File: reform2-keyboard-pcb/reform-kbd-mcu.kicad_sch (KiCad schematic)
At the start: 31 parts, among them J1 USB, J2 UART, J3 AUX, J4 USB, SW83 RESET, SW84 SW_DIP_x01, U1 ATMEGA32U4-AU, U3 MCP1700-3302E_SOT23, Y1 16MHz

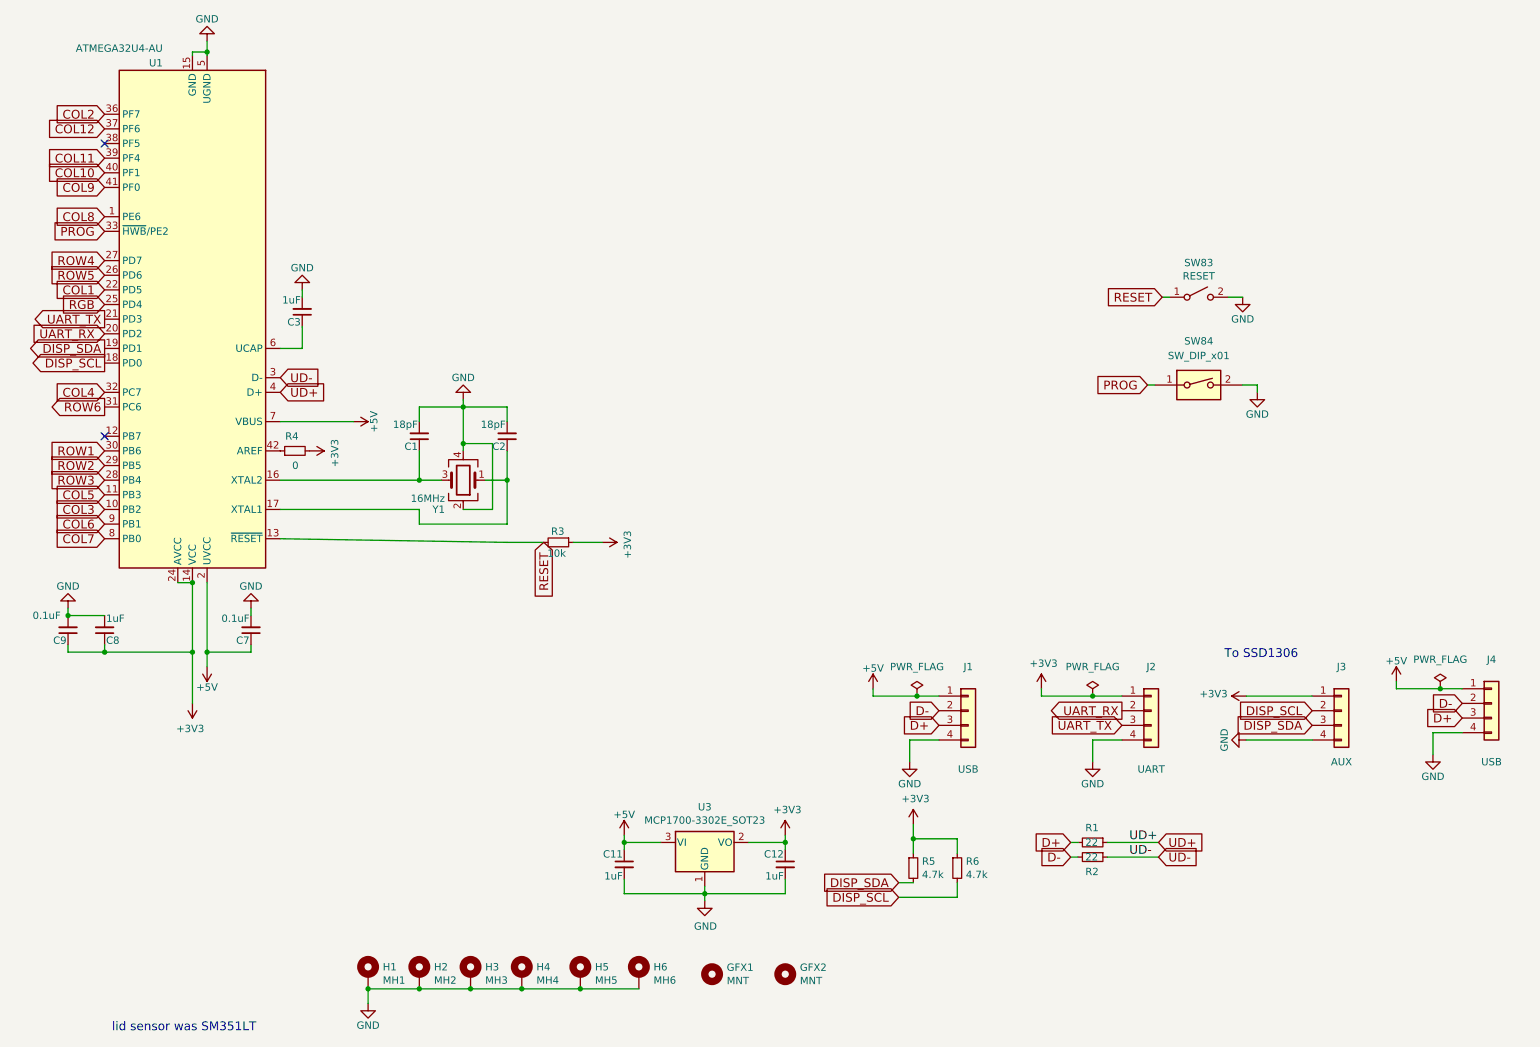
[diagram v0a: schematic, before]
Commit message: more routing of smd parts, add sockets
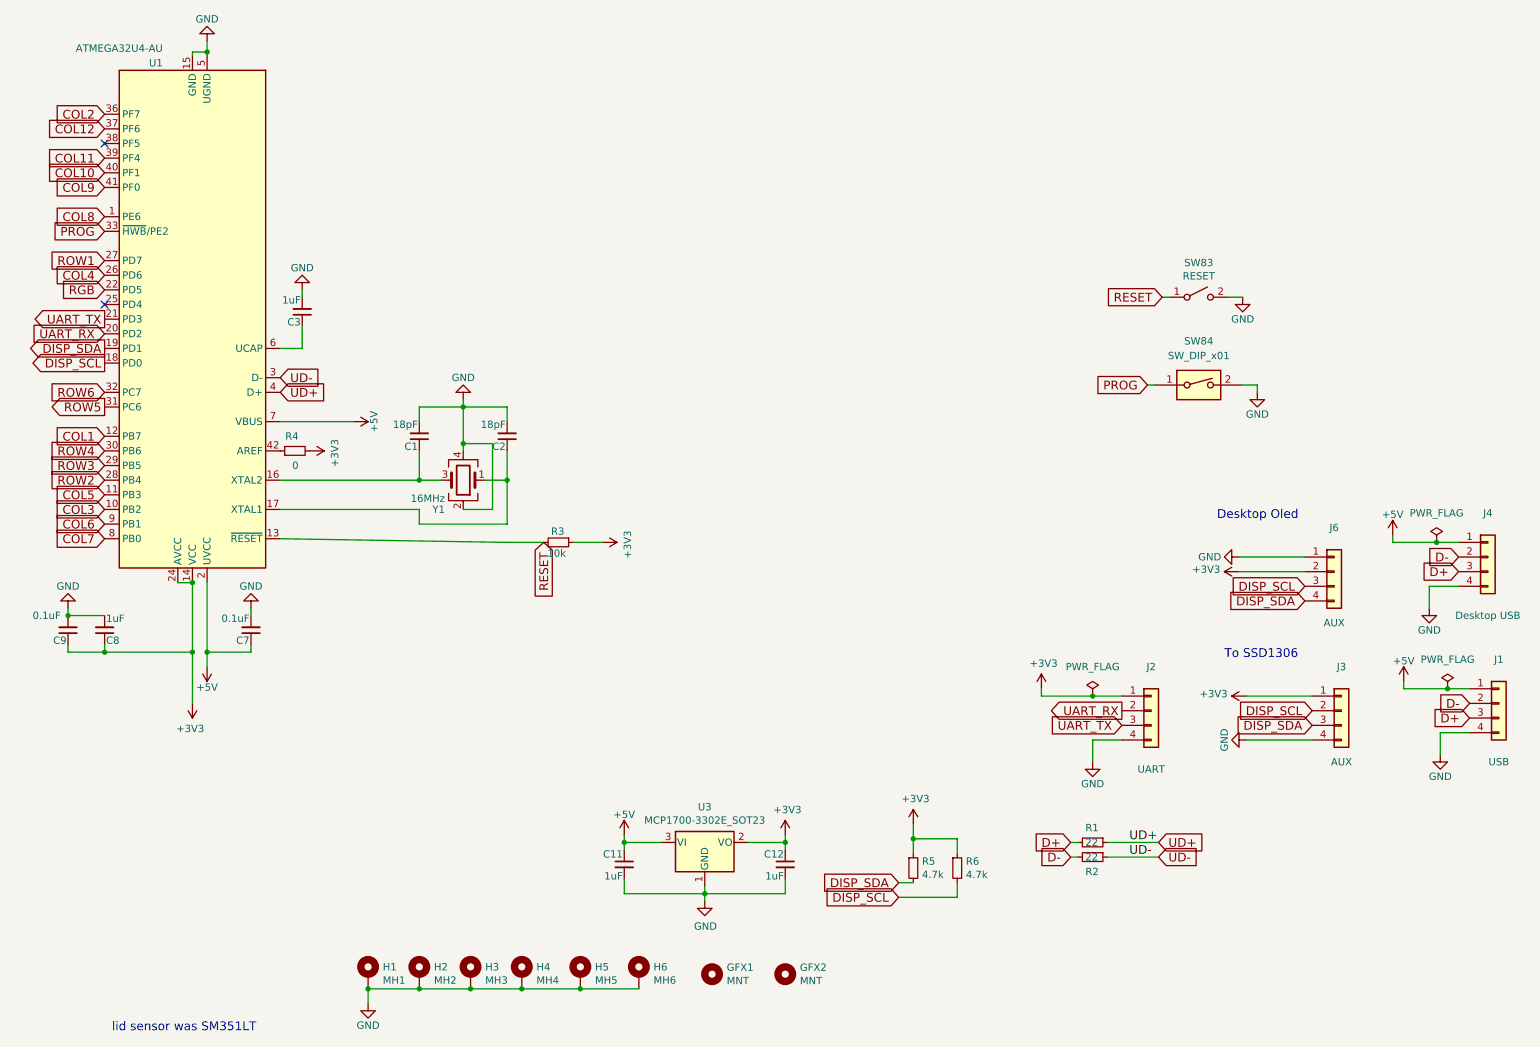
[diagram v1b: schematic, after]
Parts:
- added J6: AUX, Connector_PinHeader_2.54mm:PinHeader_1x04_P2.54mm_Vertical, symbol Connector_Generic:Conn_01x04
- J4: value USB -> Desktop USB; Manufacturer JST -> (none); Manufacturer_No S4B-PH-SM4-TB(LF)(SN) -> IDC 2.54 header 1x04
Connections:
- net +3V3: now also J6.2 (Pin_2)
- net COL1: now also U1.12 (PB7); no longer U1.22 (PD5)
- net COL4: now also U1.26 (PD6); no longer U1.32 (PC7)
- net DISP_SCL: now also J6.3 (Pin_3)
- net DISP_SDA: now also J6.4 (Pin_4)
- net GND: now also J6.1 (Pin_1)
- net RGB: now also U1.22 (PD5); no longer U1.25 (PD4)
- net ROW1: now also U1.27 (PD7); no longer U1.30 (PB6)
- net ROW2: now also U1.28 (PB4); no longer U1.29 (PB5)
- net ROW3: now also U1.29 (PB5); no longer U1.28 (PB4)
- net ROW4: now also U1.30 (PB6); no longer U1.27 (PD7)
- net ROW5: now also U1.31 (PC6); no longer U1.26 (PD6)
- net ROW6: now also U1.32 (PC7); no longer U1.31 (PC6)
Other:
- note added: "Desktop Oled"
- moved on the sheet: J1, J4

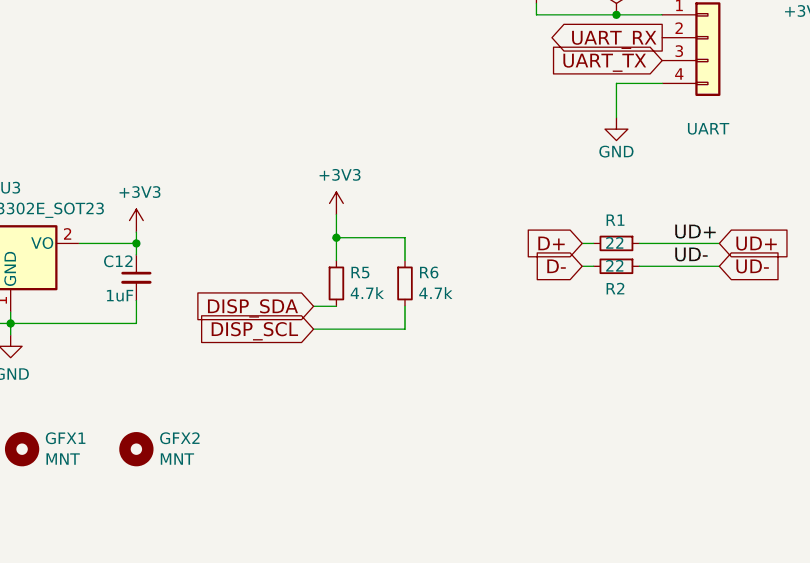
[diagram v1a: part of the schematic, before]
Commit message: change parts for better handsolders
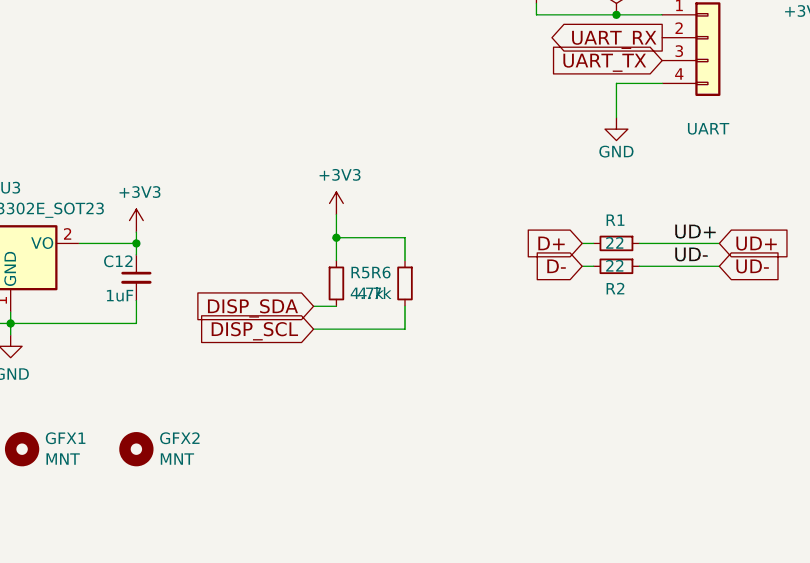
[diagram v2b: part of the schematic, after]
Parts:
- C1, C11, C12, C2, C3, C7, C8, C9: footprint Capacitor_SMD:C_0603_1608Metric -> Capacitor_SMD:C_0805_2012Metric_Pad1.18x1.45mm_HandSolder
- R1, R2, R3, R4, R5, R6: footprint Resistor_SMD:R_0603_1608Metric -> Resistor_SMD:R_0805_2012Metric_Pad1.20x1.40mm_HandSolder
- Y1: footprint Crystal:Crystal_SMD_3225-4Pin_3.2x2.5mm -> Crystal:Crystal_SMD_3225-4Pin_3.2x2.5mm_HandSoldering
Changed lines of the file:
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@@
       (effects (font (size 1.27 1.27)) (justify left))
     )
-    (property "Footprint" "Resistor_SMD:R_0603_1608Metric" (id 2) (at 195.58 160.02 0)
+    (property "Footprint" "Resistor_SMD:R_0805_2012Metric_Pad1.20x1.40mm_HandSolder" (id 2) (at 195.58 160.02 0)
       (effects (font (size 1.27 1.27)) hide)
     )
@@
       (effects (font (size 1.27 1.27)) (justify left))
     )
-    (property "Footprint" "Resistor_SMD:R_0603_1608Metric" (id 2) (at 195.58 157.48 0)
+    (property "Footprint" "Resistor_SMD:R_0805_2012Metric_Pad1.20x1.40mm_HandSolder" (id 2) (at 195.58 157.48 0)
       (effects (font (size 1.27 1.27)) hide)
     )
@@
       (effects (font (size 1.27 1.27)) (justify left))
     )
-    (property "Footprint" "Capacitor_SMD:C_0603_1608Metric" (id 2) (at 24.13 120.65 0)
+    (property "Footprint" "Capacitor_SMD:C_0805_2012Metric_Pad1.18x1.45mm_HandSolder" (id 2) (at 24.13 120.65 0)
       (effects (font (size 1.27 1.27)) hide)
     )
@@
       (effects (font (size 1.27 1.27)) (justify left))
     )
-    (property "Footprint" "Capacitor_SMD:C_0603_1608Metric" (id 2) (at 49.53 120.65 0)
+    (property "Footprint" "Capacitor_SMD:C_0805_2012Metric_Pad1.18x1.45mm_HandSolder" (id 2) (at 49.53 120.65 0)
       (effects (font (size 1.27 1.27)) hide)
     )
@@
       (effects (font (size 1.27 1.27)) (justify left))
     )
-    (property "Footprint" "Capacitor_SMD:C_0603_1608Metric" (id 2) (at 17.78 120.65 0)
+    (property "Footprint" "Capacitor_SMD:C_0805_2012Metric_Pad1.18x1.45mm_HandSolder" (id 2) (at 17.78 120.65 0)
       (effects (font (size 1.27 1.27)) hide)
     )
@@
       (effects (font (size 1.27 1.27)) (justify left))
     )
-    (property "Footprint" "Resistor_SMD:R_0603_1608Metric" (id 2) (at 164.465 161.925 0)
+    (property "Footprint" "Resistor_SMD:R_0805_2012Metric_Pad1.20x1.40mm_HandSolder" (id 2) (at 164.465 161.925 0)
       (effects (font (size 1.27 1.27)) hide)
     )
@@
     (pin "2")
   )
-  (symbol (lib_id "reform2-keyboard-rescue:R_Small-Device") (at 172.085 161.925 0) (unit 1)
-    (in_bom yes) (on_board yes)
-    (property "Reference" "R6" (id 0) (at 173.5836 160.7566 0)
-      (effects (font (size 1.27 1.27)) (justify left))
-    )
-    (property "Value" "4.7k" (id 1) (at 173.5836 163.068 0)
-      (effects (font (size 1.27 1.27)) (justify left))
-    )
-    (property "Footprint" "Resistor_SMD:R_0603_1608Metric" (id 2) (at 172.085 161.925 0)
+  (symbol (lib_id "reform2-keyboard-rescue:R_Small-Device") (at 172.085 161.925 0) (mirror y) (unit 1)
+    (in_bom yes) (on_board yes)
+    (property "Reference" "R6" (id 0) (at 170.5864 160.7566 0)
+      (effects (font (size 1.27 1.27)) (justify left))
+    )
+    (property "Value" "4.7k" (id 1) (at 170.5864 163.068 0)
+      (effects (font (size 1.27 1.27)) (justify left))
+    )
+    (property "Footprint" "Resistor_SMD:R_0805_2012Metric_Pad1.20x1.40mm_HandSolder" (id 2) (at 172.085 161.925 0)
       (effects (font (size 1.27 1.27)) hide)
     )
@@
       (effects (font (size 1.27 1.27)) (justify left))
     )
-    (property "Footprint" "Capacitor_SMD:C_0603_1608Metric" (id 2) (at 114.3 161.29 0)
+    (property "Footprint" "Capacitor_SMD:C_0805_2012Metric_Pad1.18x1.45mm_HandSolder" (id 2) (at 114.3 161.29 0)
       (effects (font (size 1.27 1.27)) hide)
     )
@@
       (effects (font (size 1.27 1.27)) (justify left))
     )
-    (property "Footprint" "Capacitor_SMD:C_0603_1608Metric" (id 2) (at 142.24 161.29 0)
+    (property "Footprint" "Capacitor_SMD:C_0805_2012Metric_Pad1.18x1.45mm_HandSolder" (id 2) (at 142.24 161.29 0)
       (effects (font (size 1.27 1.27)) hide)
     )
@@
       (effects (font (size 1.27 1.27)) (justify left))
     )
-    (property "Footprint" "Crystal:Crystal_SMD_3225-4Pin_3.2x2.5mm" (id 2) (at 86.36 94.615 0)
+    (property "Footprint" "Crystal:Crystal_SMD_3225-4Pin_3.2x2.5mm_HandSoldering" (id 2) (at 86.36 94.615 0)
       (effects (font (size 1.27 1.27)) hide)
     )
@@
       (effects (font (size 1.27 1.27)) (justify left))
     )
-    (property "Footprint" "Capacitor_SMD:C_0603_1608Metric" (id 2) (at 78.74 86.995 0)
+    (property "Footprint" "Capacitor_SMD:C_0805_2012Metric_Pad1.18x1.45mm_HandSolder" (id 2) (at 78.74 86.995 0)
       (effects (font (size 1.27 1.27)) hide)
     )
@@
       (effects (font (size 1.27 1.27)) (justify left))
     )
-    (property "Footprint" "Resistor_SMD:R_0603_1608Metric" (id 2) (at 102.87 105.41 0)
+    (property "Footprint" "Resistor_SMD:R_0805_2012Metric_Pad1.20x1.40mm_HandSolder" (id 2) (at 102.87 105.41 0)
       (effects (font (size 1.27 1.27)) hide)
     )
@@
       (effects (font (size 1.27 1.27)) (justify left))
     )
-    (property "Footprint" "Capacitor_SMD:C_0603_1608Metric" (id 2) (at 58.42 65.405 0)
+    (property "Footprint" "Capacitor_SMD:C_0805_2012Metric_Pad1.18x1.45mm_HandSolder" (id 2) (at 58.42 65.405 0)
       (effects (font (size 1.27 1.27)) hide)
     )
@@
       (effects (font (size 1.27 1.27)) (justify left))
     )
-    (property "Footprint" "Resistor_SMD:R_0603_1608Metric" (id 2) (at 57.15 89.535 0)
+    (property "Footprint" "Resistor_SMD:R_0805_2012Metric_Pad1.20x1.40mm_HandSolder" (id 2) (at 57.15 89.535 0)
       (effects (font (size 1.27 1.27)) hide)
     )
@@
       (effects (font (size 1.27 1.27)) (justify left))
     )
-    (property "Footprint" "Capacitor_SMD:C_0603_1608Metric" (id 2) (at 93.98 86.995 0)
-      (effects (font (size 1.27 1.27)) hide)
-    )
+    (property "Footprint" "Capacitor_SMD:C_0805_2012Metric_Pad1.18x1.45mm_HandSolder" (id 2) (at 93.98 86.995 0)
+      (effects (font (size 1.27 1.27)) hide)
+    )
